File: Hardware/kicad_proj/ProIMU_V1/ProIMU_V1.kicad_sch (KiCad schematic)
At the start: 36 parts, among them J1 Conn_02x03_Counter_Clockwise, J4 502570-0893, U1 ADM101E, U2 ISO1050DUB, U4 AIR602, U5 BMP280, U6 MPU-9250, U9 L80-M39

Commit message: Removed isolated DC-DC converter and added new regulator in place of it
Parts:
- added D? (x2): DIODE, symbol Simulation_SPICE:DIODE
- added R? (x4): 1K, Resistor_SMD:R_0402_1005Metric_Pad0.72x0.64mm_HandSolder, symbol Device:R_Small
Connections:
- net Battery/D+: no longer D1.1 (K), R13.1
- net Battery/D-: no longer D1.2 (K), R12.2
- net GND: now also R?.1, R?.1
- net MCU/CAN1_RX: no longer U2.2 (RXD)
- net MCU/CAN1_TX: no longer U2.3 (TXD)
- net VDD: now also D?.2 (K), D?.2 (K); no longer C2.2, CAN1.1 (Pin_1), USB1.A4_B9 (VBUS), USB1.B4_A9 (VBUS)
- new net: D1.2 (K), R12.2
- new net: C2.2, D?.1 (A), R?.2, USB1.A4_B9 (VBUS), USB1.B4_A9 (VBUS)
- new net: CAN1.1 (Pin_1), D?.1 (A), R?.2
- new net: D1.1 (K), R13.1
- new net CAN_POWER_IND: R?.1, R?.2
- new net USB_POWER_IND: R?.1, R?.2
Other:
- moved on the sheet: C2, C3, C5, CAN1, D1, R1, R12, R13, R2, R4, R7, U2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

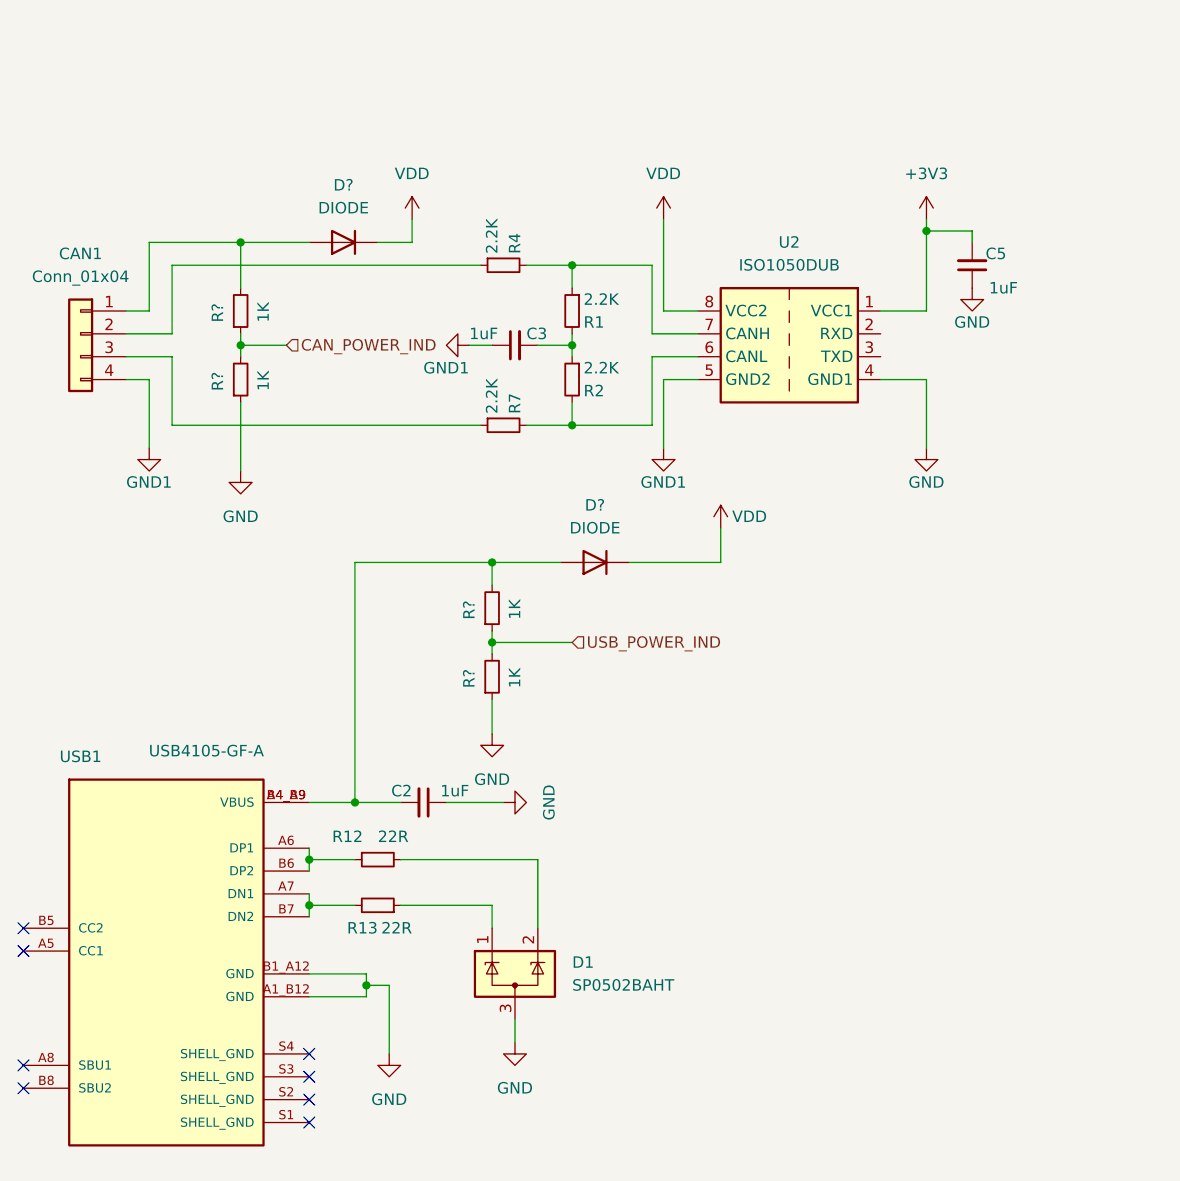
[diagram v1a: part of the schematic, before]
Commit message: Added new schematic for USB and CAN
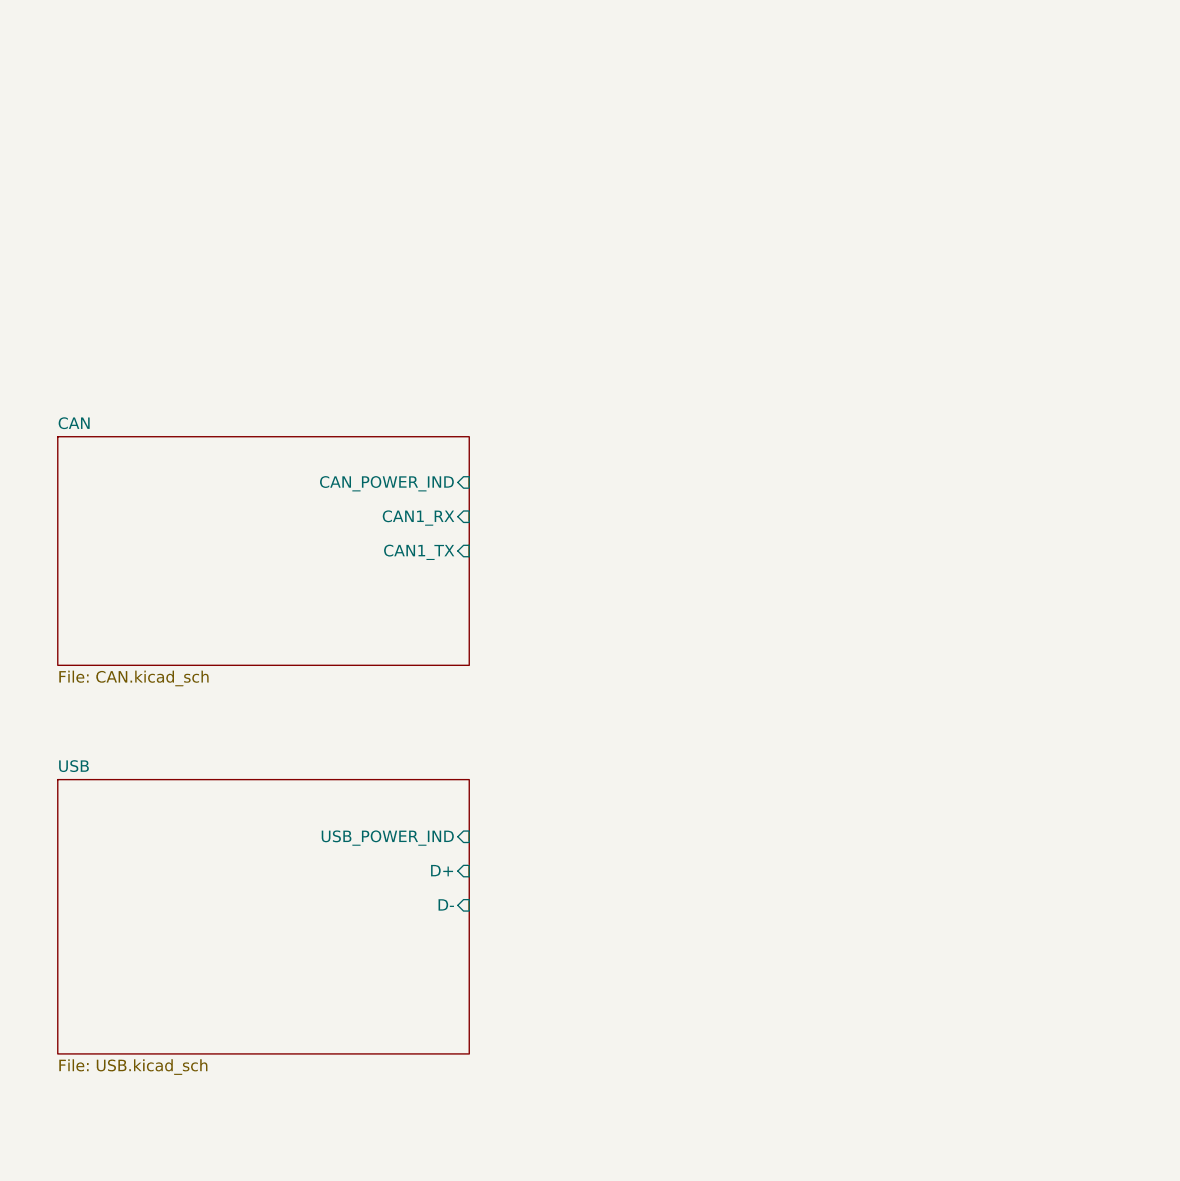
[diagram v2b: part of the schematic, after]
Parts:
- removed C2, C3, C5: 1uF, Capacitor_SMD:C_0402_1005Metric_Pad0.74x0.62mm_HandSolder, symbol Device:C_Small
- removed CAN1: Conn_01x04, Connector_JST:JST_PH_S4B-PH-SM4-TB_1x04-1MP_P2.00mm_Horizontal, symbol Connector_Generic:Conn_01x04
- removed D1: SP0502BAHT, Package_TO_SOT_SMD:SOT-23, symbol Power_Protection:SP0502BAHT
- removed D? (x2): DIODE, symbol Simulation_SPICE:DIODE
- removed R1, R2, R4, R7: 2.2K, Resistor_SMD:R_0402_1005Metric_Pad0.72x0.64mm_HandSolder, symbol Device:R_Small
- removed R12, R13: 22R, Resistor_SMD:R_0402_1005Metric_Pad0.72x0.64mm_HandSolder, symbol Device:R_Small
- removed R? (x4): 1K, Resistor_SMD:R_0402_1005Metric_Pad0.72x0.64mm_HandSolder, symbol Device:R_Small
- removed U2: ISO1050DUB, Package_SO:SOP-8_6.62x9.15mm_P2.54mm, symbol Interface_CAN_LIN:ISO1050DUB
- removed USB1: USB4105-GF-A, footprints:GCT_USB4105-GF-A, symbol USB4105-GF-A:USB4105-GF-A
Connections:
- no-connect marks 22 -> 14
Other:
- added sheet CAN (CAN.kicad_sch)
- added sheet USB  (USB.kicad_sch)

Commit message: Added new schematic for Radio and Isolated UART
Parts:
- removed C21, C22, C4: 1uF, Capacitor_SMD:C_0402_1005Metric_Pad0.74x0.62mm_HandSolder, symbol Device:C_Small
- removed RS232: Conn_01x04, Connector_JST:JST_PH_S4B-PH-SM4-TB_1x04-1MP_P2.00mm_Horizontal, symbol Connector_Generic:Conn_01x04
- removed U1: ADM101E, Package_SO:MSOP-10_3x3mm_P0.5mm, symbol Interface_UART:ADM101E
- removed U4: AIR602, footprints:AIR602, symbol air602:AIR602
- removed U9: L80-M39, footprints:XCVR_L80-M39, symbol L80-M39:L80-M39
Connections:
- no-connect marks 14 -> 4
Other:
- added sheet Isolated UART (UART.kicad_sch)
- added sheet Radio (Radio.kicad_sch)
- sheet Battery ports: added CHARGER_TURN_OFF; removed D+, D-, INT, OTG, SCL, SDA, SYSTEM_OUT, USB_PWR_IN, nCE

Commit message: Added sensor schematic
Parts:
- removed C10, C6, C9: 100nF, Capacitor_SMD:C_0402_1005Metric_Pad0.74x0.62mm_HandSolder, symbol Device:C_Small
- removed C11: 10nF, Capacitor_SMD:C_0402_1005Metric_Pad0.74x0.62mm_HandSolder, symbol Device:C_Small
- removed C7, C8: 0.1uF, Capacitor_SMD:C_0402_1005Metric_Pad0.74x0.62mm_HandSolder, symbol Device:C_Small
- removed J1: Conn_02x03_Counter_Clockwise, Connector_PinHeader_2.54mm:PinHeader_2x03_P2.54mm_Vertical_SMD, symbol Connector_Generic:Conn_02x03_Counter_Clockwise
- removed J4: 502570-0893, footprints:MOLEX_502570-0893, symbol 502570-0893:502570-0893
- removed R5, R6: 2.2K, Resistor_SMD:R_0402_1005Metric_Pad0.72x0.64mm_HandSolder, symbol Device:R_Small
- removed U5: BMP280, footprints:BMP280, symbol 2022-02-05_19-44-07:BMP280
- removed U6: MPU-9250, QFN40P300X300X105-24N, symbol MPU-9250:MPU-9250
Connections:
- no-connect marks 4 -> 0
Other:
- added sheet Sensor (Sensor.kicad_sch)
- sheet MCU ports: added none; removed BMP280_I2C1_SCL, BMP280_I2C1_SDA, CAN1_RX, CAN1_TX, CAN_SHUTDOWN, CHARGER_I2C2_SDA, CHARGER_OTG, CHARGER_nCE, DEBUG_SWCLK, DEBUG_SWDIO, DEBUG_UART1_RX, DEBUG_UART1_TX, FUEL_GAUGE_I2C2_SDA, FUEL_GAUGE_SCL, GPS_RESET, GPS_UART6_RX, GPS_UART6_TX, MPU9250_INT_EXTI4, MPU9250_SPI1_MISO, MPU9250_SPI1_MOSI, MPU9250_SPI1_SCK, MPU9250_SPI1_nCSS, NRST, RS232_UART3_RX, RS232_UART3_TX, SDCARD_DET_LEVEL, SDCARD_DET_SWT, SDCARD_SDIO_CLK, SDCARD_SDIO_CMD, SDCARD_SDIO_D0, SDCARD_SDIO_D1, SDCARD_SDIO_D2, SDCARD_SDIO_D3, USB+, USB-, WIFI_RESET, WIFI_UART2_RX, WIFI_UART2_TX
- moved on the sheet: H1, H2, H3, H4

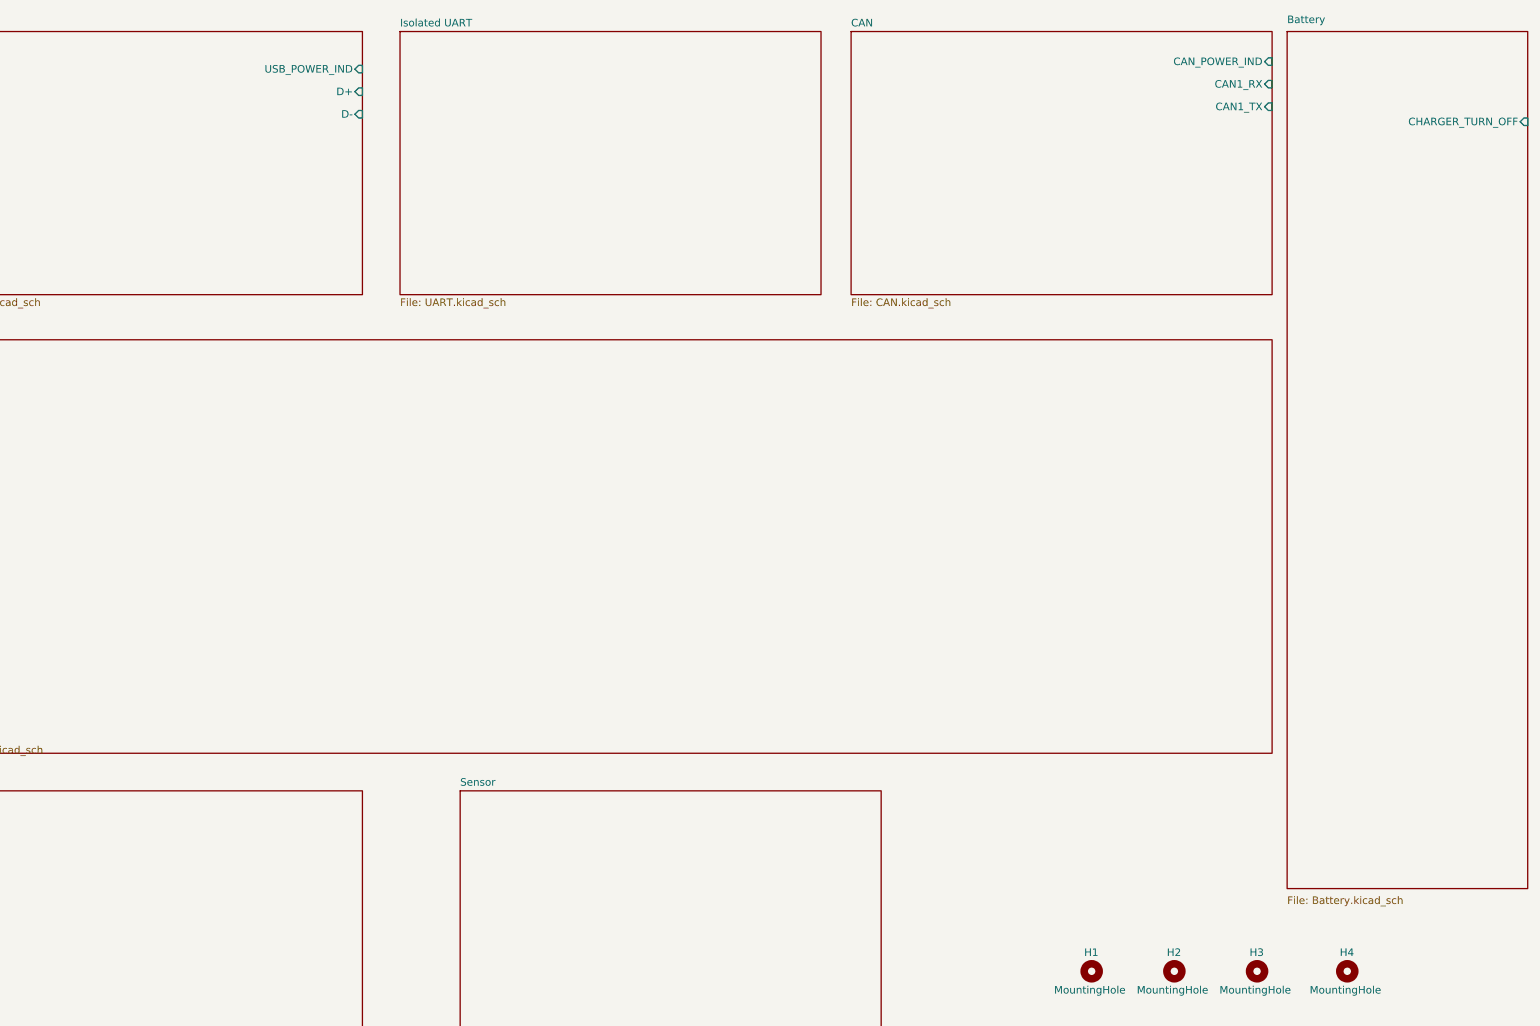
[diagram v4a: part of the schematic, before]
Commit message: Updated schematic and removed redundant schematic
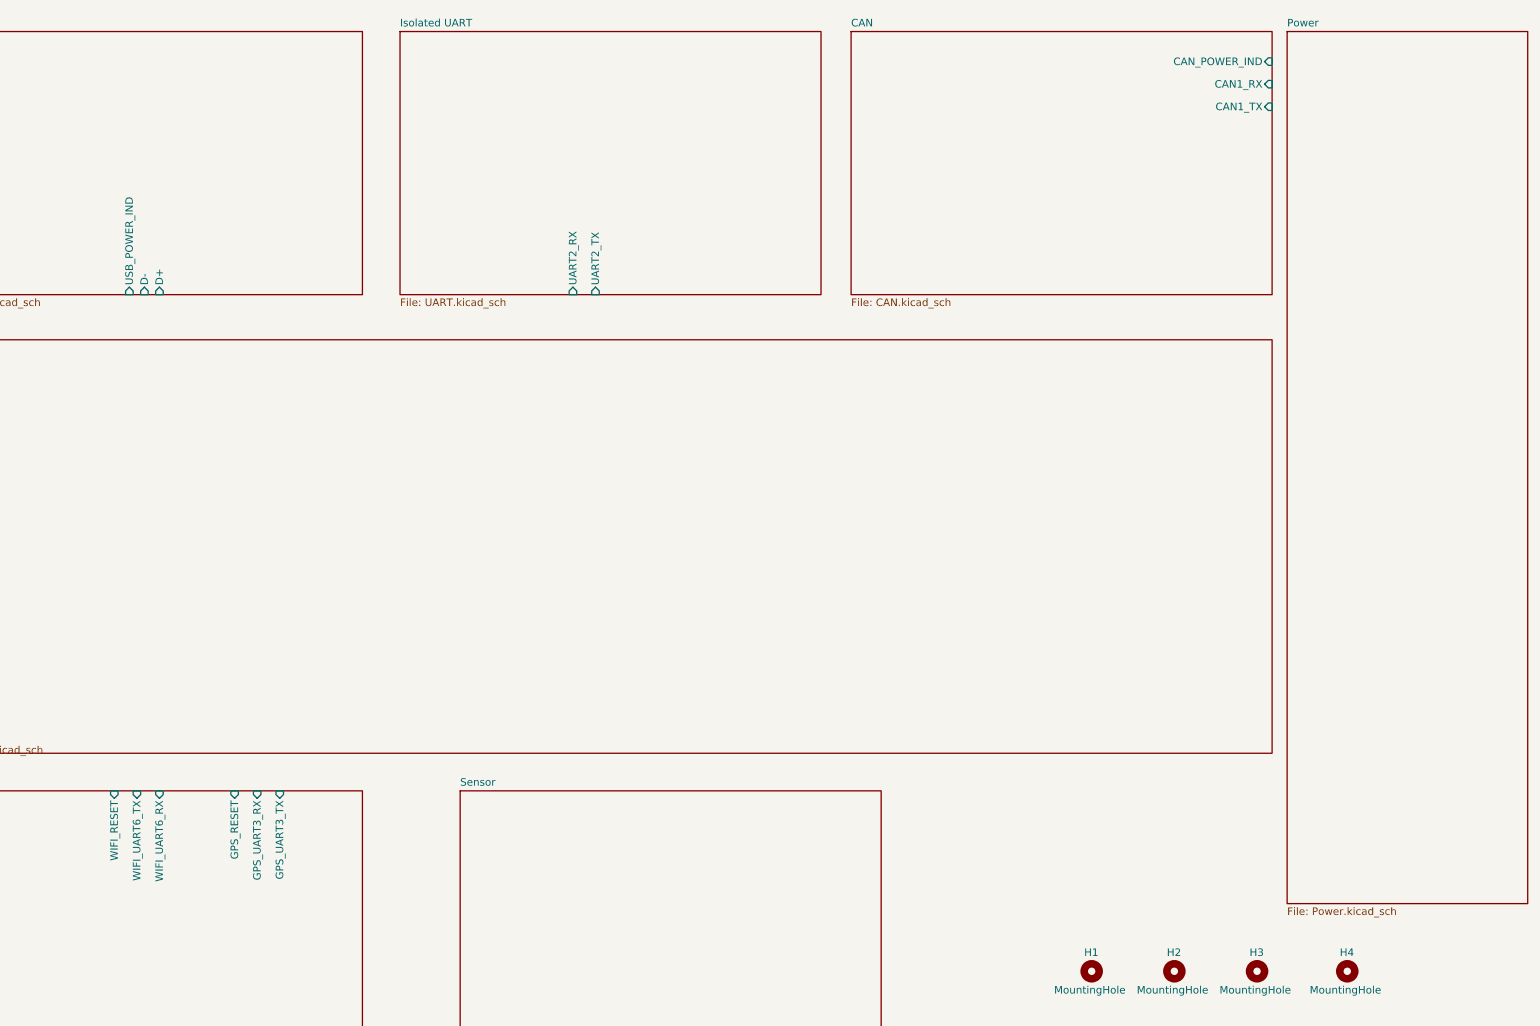
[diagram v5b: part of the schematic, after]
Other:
- removed sheet Battery
- added sheet Power (Power.kicad_sch)
- sheet Isolated UART ports: added UART2_RX, UART2_TX; removed none
- sheet Radio ports: added GPS_RESET, GPS_UART3_RX, GPS_UART3_TX, WIFI_RESET, WIFI_UART6_RX, WIFI_UART6_TX; removed none

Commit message: Updated Repo
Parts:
- added BAT?: Conn_01x03, symbol Connector_Generic:Conn_01x03
- added C? (x9): 1uF, Capacitor_SMD:C_0402_1005Metric_Pad0.74x0.62mm_HandSolder, symbol Device:C_Small
- added C? (x7): C, Capacitor_SMD:C_0805_2012Metric_Pad1.18x1.45mm_HandSolder, symbol Device:C
- added C? (x2): 0.1uF, Capacitor_SMD:C_0402_1005Metric_Pad0.74x0.62mm_HandSolder, symbol Device:C_Small
- added C? (x2): 4.7uF, Capacitor_SMD:C_0402_1005Metric_Pad0.74x0.62mm_HandSolder, symbol Device:C_Small
- added C? (x2): 100nF, Capacitor_SMD:C_0402_1005Metric_Pad0.74x0.62mm_HandSolder, symbol Device:C_Small
- added C?: 10nF, Capacitor_SMD:C_0402_1005Metric_Pad0.74x0.62mm_HandSolder, symbol Device:C_Small
- added D? (x2): LED, symbol Device:LED
- added D?: SP0502BAHT, Package_TO_SOT_SMD:SOT-23, symbol Power_Protection:SP0502BAHT
- added J?: Conn_02x03_Counter_Clockwise, Connector_PinHeader_2.54mm:PinHeader_2x03_P2.54mm_Vertical_SMD, symbol Connector_Generic:Conn_02x03_Counter_Clockwise
- added J?: 502570-0893, footprints:MOLEX_502570-0893, symbol 502570-0893:502570-0893
- added L?: L, symbol Device:L
- added R? (x2): 2.2K, Resistor_SMD:R_0402_1005Metric_Pad0.72x0.64mm_HandSolder, symbol Device:R_Small
- added R? (x2): 22R, Resistor_SMD:R_0402_1005Metric_Pad0.72x0.64mm_HandSolder, symbol Device:R_Small
- added R? (x3): 1K, Resistor_SMD:R_0402_1005Metric_Pad0.72x0.64mm_HandSolder, symbol Device:R_Small
- added R?: 1.13K, Resistor_SMD:R_0402_1005Metric_Pad0.72x0.64mm_HandSolder, symbol Device:R_Small
- added R? (x2): 10K, Resistor_SMD:R_0402_1005Metric_Pad0.72x0.64mm_HandSolder, symbol Device:R_Small
- added R?: 1.18K, Resistor_SMD:R_0402_1005Metric_Pad0.72x0.64mm_HandSolder, symbol Device:R_Small
- added U?: MPU-9250, QFN40P300X300X105-24N, symbol MPU-9250:MPU-9250
- added U?: L80-M39, footprints:XCVR_L80-M39, symbol L80-M39:L80-M39
- added U?: BMP280, footprints:BMP280, symbol 2022-02-05_19-44-07:BMP280
- added U?: AIR602, footprints:AIR602, symbol air602:AIR602
- added U?: STM32F411CEUx, Package_DFN_QFN:QFN-48-1EP_7x7mm_P0.5mm_EP5.6x5.6mm, symbol MCU_ST_STM32F4:STM32F411CEUx
- added U?: TPS63000, Package_SON:Texas_DRC0010J_ThermalVias, symbol Regulator_Switching:TPS63000
- added U?: BQ24075RGT, Package_DFN_QFN:VQFN-16-1EP_3x3mm_P0.5mm_EP1.6x1.6mm, symbol Battery_Management:BQ24075RGT
- added U?: SPX2920M3-3.3_SOT223, Package_TO_SOT_SMD:SOT-223-3_TabPin2, symbol Regulator_Linear:SPX2920M3-3.3_SOT223
- added USB?: USB4105-GF-A, footprints:GCT_USB4105-GF-A, symbol USB4105-GF-A:USB4105-GF-A
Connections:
- new net: R?.1, U?.21 (PB10), U?.4 (SCK)
- new net: J?.2 (Pin_2), U?.34 (PA13)
- new net: J?.3 (Pin_3), U?.37 (PA14)
- new net: C?.1, U?.10 (REGOUT)
- new net: U?.23 (SCL/SCLK), U?.42 (PB6)
- new net: U?.24 (SDA/SDI), U?.46 (PB9)
- new net: R?.1, USB?.A6 (DP1), USB?.B6 (DP2)
- new net: D?.2 (K), R?.2, U?.33 (PA12)
- new net: D?.2 (A), R?.1 (x2)
- new net: U?.1 (RXD1), U?.38 (PA15)
- new net: U?.2 (TXD1), U?.31 (PA10)
- new net: U?.12 (RES), U?.14 (PA4)
- new net: U?.13 (PA3), U?.5 (TX0)
- new net: U?.12 (PA2), U?.6 (RX0)
- new net: J?.DS (DET_SWT), U?.15 (PA5)
- new net: J?.3 (CMD), U?.16 (PA6)
- new net: J?.DL (DET_LEVEL), U?.17 (PA7)
- new net: C?.1, U?.22 (VCAP1)
- new net: J?.8 (DAT1), U?.29 (PA8)
- new net: J?.1 (DAT2), U?.30 (PA9)
- new net: D?.1 (K), R?.1, U?.32 (PA11)
- new net: R?.2, U?.44 (BOOT0)
- new net: D?.1 (K), U?.9 (~{CHG})
- new net: BAT?.1 (Pin_1), C?.2, U?.2 (BAT), U?.3 (BAT)
- new net: BAT?.2 (Pin_2), U?.1 (TS)
- new net: L?.2, U?.2 (L2)
- new net: L?.1, U?.4 (L1)
- new net: C?.1, R?.2, U?.5 (VIN)
- new net: C?.1, R?.1, U?.6 (EN), U?.7 (PS/SYNC), U?.8 (VINA)
- new net: C?.2, USB?.A4_B9 (VBUS), USB?.B4_A9 (VBUS)
- new net: R?.2, U?.12 (ILIM)
- new net: R?.2, U?.16 (ISET)
- new net: D?.1 (K), U?.7 (~{PGOOD})
- new net: R?.2, USB?.A7 (DN1), USB?.B7 (DN2)
- new net +3V3: C?.1, C?.1, C?.1, C?.1, C?.1, C?.1, C?.1, C?.1, C?.1, J?.4 (VDD), R?.1, R?.2, R?.2, R?.2, U?.1 (RESV_1), U?.1 (VBAT), U?.2 (CSB), U?.22 (~{CS}), U?.24 (VDD), U?.3 (VO), U?.36 (VDD), U?.4 (VCC), U?.4 (VCC), U?.48 (VDD), U?.5 (V_BCKP), U?.6 (VDDIO), U?.8 (VDDIO), U?.9 (VDDA)
- new net +5V: C?.1, C?.1, C?.1, C?.1, C?.1, C?.1, U?.1 (VI), U?.1 (VOUT), U?.10 (FB), U?.13 (VDD), U?.8 (VDD)
- new net ANT: U?.2 (ANT)
- new net GND: BAT?.3 (Pin_3), C?.1, C?.1, C?.1, C?.1, C?.2, C?.2, C?.2, C?.2, C?.2, C?.2, C?.2, C?.2, C?.2, C?.2, C?.2, C?.2, C?.2, C?.2, C?.2, C?.2, C?.2, C?.2, C?.2, D?.3 (A), J?.6 (VSS), R?.1, R?.1, U?.1 (GND), U?.1 (GND), U?.11 (PGND), U?.12 (GND), U?.17 (VSS), U?.18 (GND), U?.2 (GND), U?.20 (RESV_20), U?.23 (VSS), U?.3 (GND), U?.3 (GND), U?.3 (PGND), U?.35 (VSS), U?.47 (VSS), U?.49 (VSS), U?.5 (SDO), U?.7 (GND), U?.8 (VSS), U?.8 (VSSA), U?.9 (GND), USB?.A1_B12 (GND), USB?.B1_A12 (GND)
- new net I2C2_SDA: R?.1, U?.3 (SDI), U?.39 (PB3)
- new net NRST: J?.1 (Pin_1), R?.1, U?.7 (NRST)
- new net SDIO_CK: J?.5 (CLK), U?.28 (PB15)
- new net SDIO_D0: J?.7 (DAT0), U?.43 (PB7)
- new net SDIO_D3: J?.2 (CD/DAT3), U?.41 (PB5)
- new net VCC: C?.2, R?.2, R?.2, U?.10 (OUT), U?.11 (OUT), U?.5 (EN2), U?.6 (EN1)
- new net VDD: C?.2, U?.13 (IN)
- no-connect marks 0 -> 23
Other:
- removed sheet CAN
- removed sheet Isolated UART
- removed sheet MCU
- removed sheet Power
- removed sheet Radio
- removed sheet Sensor
- removed sheet USB 

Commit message: Updated Schematic and Layout
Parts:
- gave numbers to parts that had none: 50
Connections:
- net at U3.17 (PA7): no longer J2.DL (DET_LEVEL)
- net SD_DET_LEVEL: now reaches U3.45 (PB8)
- net SD_DET_LEVEL: now also J2.DL (DET_LEVEL)
